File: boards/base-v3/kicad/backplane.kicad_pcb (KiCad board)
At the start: 6 copper layers, 122 x 122 mm, 226 parts, among them J1 ME1022410103011 Mini Cool Edg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, J11 MEG300 84501 GPU face (pinout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, J12 MEG300 84501 SSD face (base-s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, J13 MEG300 84501 I/O face (base-i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, J14 MCIO 124P RA (C4867471) -> Fa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, J3 BM15B-GHS-TBT (C5305069) Face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, J4 BM15B-GHS-TBT (C5305069) Face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, J8 BM03B-SRSS-TB SWD (DNP), Q1 AO3401A P-MOS, Q10 2N7002 N-MOS, Q11 2N7002 N-MOS, Q12 2N7002 N-MOS, Q2 AO3401A P-MOS, Q5 AO3401A P-MOS, Q6 AO3401A P-MOS, Q7 AO3401A P-MOS, Q8 AO3401A P-MOS, SW1 BOOTSEL (TS-1187A), SW2 BENCH power button (TS-1187A), U1 RP2350B QFN-80 (C42415655), U2 W25Q128JVSIQ (C97521, basic), U20 DS320PR1601ZDGR, U21 DS320PR810NJXR, U22 DS320PR810NJXR, U24 TPS565208DDCR, U25 TPS259824LNRGE, U26 TMP1075DGKR @0x4A core side (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, U27 TSSOP-16, U3 TMP1075DGKR @0x48 core side (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, U4 TMP1075DGKR @0x49 PSU side (C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, U5 INA226AIDGSR @0x40 (C49851), U6 TPS563201DDCR (C116592) -> 3V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, U7 TPS563201DDCR (C116592) -> 5V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, U8 SN74LVC1G74DCUR thermal latch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, Y1 12MHz 3225 crystal 20pF

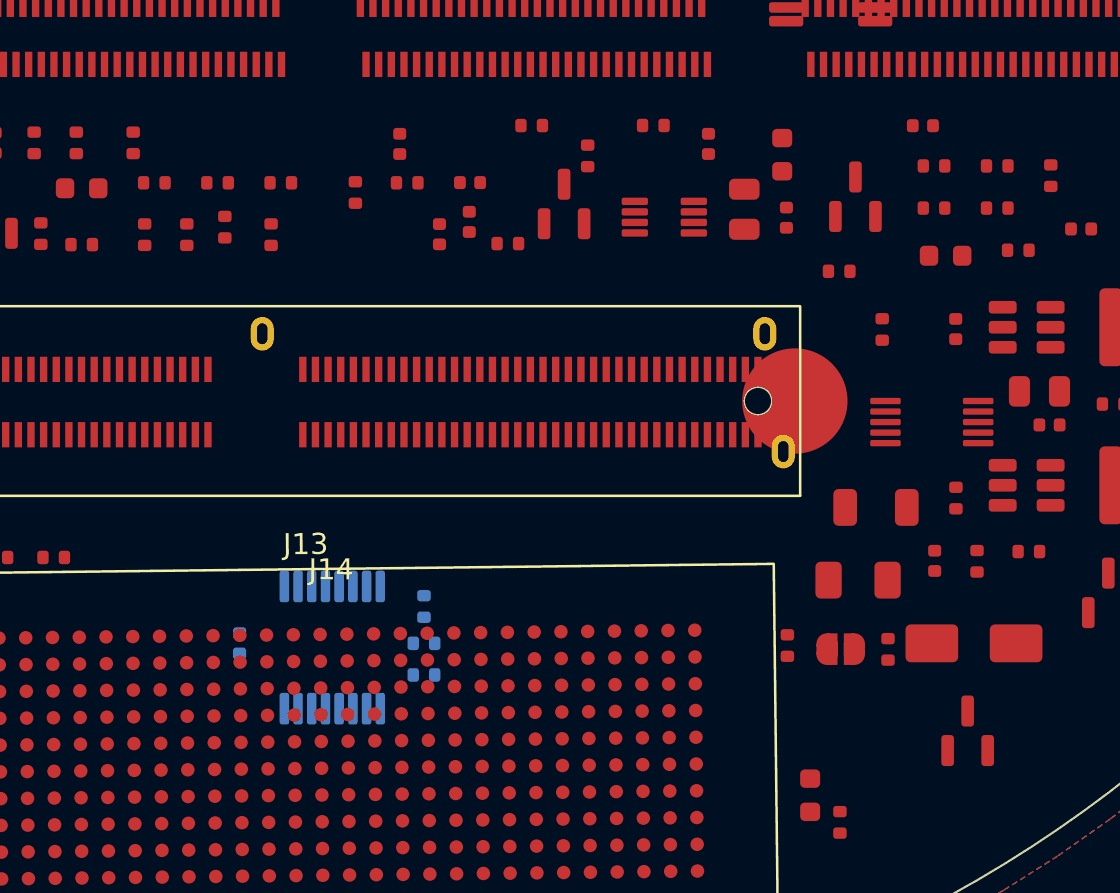
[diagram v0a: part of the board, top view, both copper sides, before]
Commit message: Sync design state 2026-10-30: base board PS_ON interlock removed from PCB, ERC 0 errors / 142 warnings, routing in progress
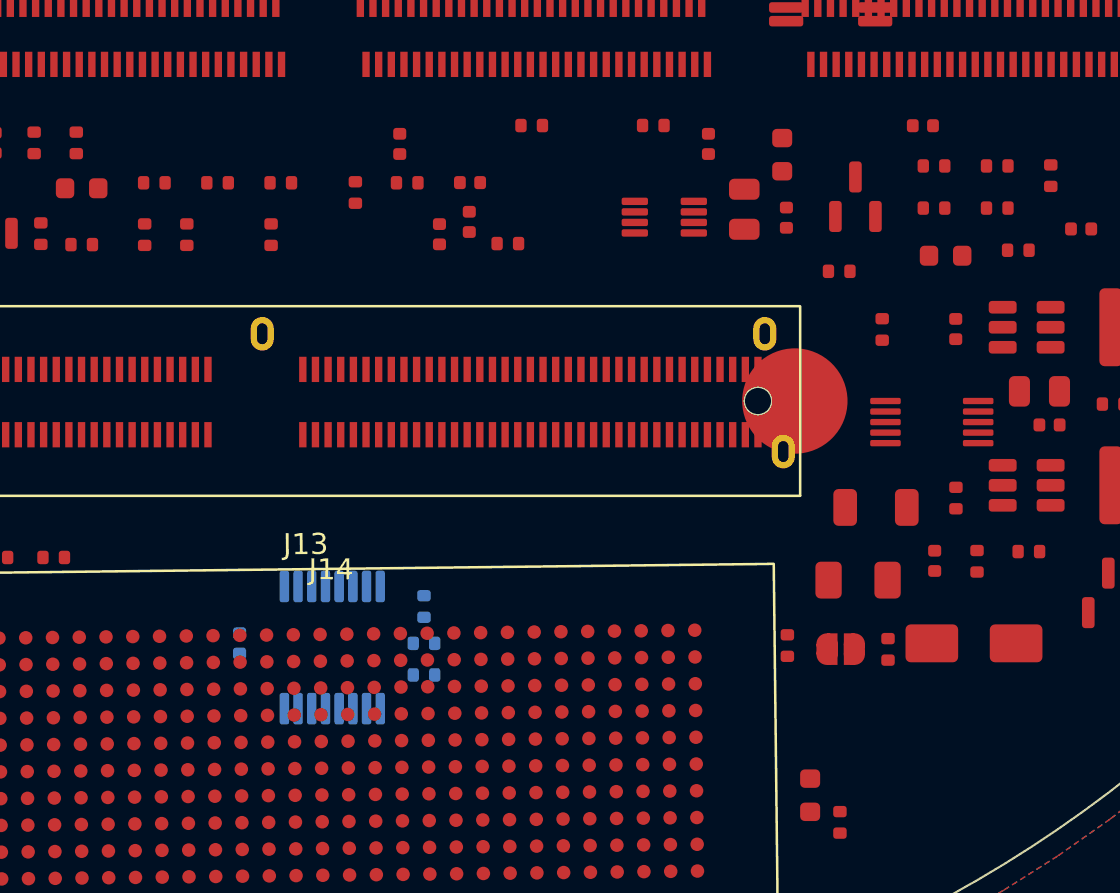
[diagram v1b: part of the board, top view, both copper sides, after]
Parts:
- removed Q7, Q8: AO3401A P-MOS, MP62_BP:SOT-23
- removed R12, R55: 100k 1% 0402, MP62_BP:R_0402_1005Metric
- removed R15: 10k 1% 0402, MP62_BP:R_0402_1005Metric
